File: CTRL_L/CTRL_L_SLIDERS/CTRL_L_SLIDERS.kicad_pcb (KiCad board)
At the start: 2 copper layers, 1 part

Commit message: Finished Volume/Brightness Slider Daugherboard!
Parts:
- removed the REF** at (126.5, 105.5)
- added J1: BM04B-NSHSS-TBT_LF__SN_, BM04B-NSHSS-TBT:BM04BNSHSSTBTLFSN, B.Cu at (190.9, 90.2)
- added REF**: M2.5_2.7mm, MountingHole:MountingHole_2.7mm_M2.5, B.Cu at (154.6, 81.2)
- added REF**: M2.5_2.7mm, MountingHole:MountingHole_2.7mm_M2.5, B.Cu at (154.6, 97.1)
- added VR1: RA2043F-20-10EB1-B10K, RA2043F-20-10EB1-B10K:RA2043F2010EB1B10K, F.Cu at (164.0, 96.2)
- added VR2: RA2043F-20-10EB1-B10K, RA2043F-20-10EB1-B10K:RA2043F2010EB1B10K, F.Cu at (164.0, 84.6)
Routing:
- net GND: track 0.00 -> 70.9 mm, vias 0 -> 1
- net SL_BRI: track 0.00 -> 32.8 mm
- net SL_VOL: track 0.00 -> 29.9 mm
- net +3V3: track 0.00 -> 18.0 mm
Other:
- board outline added: 44.2 x 23.2 mm

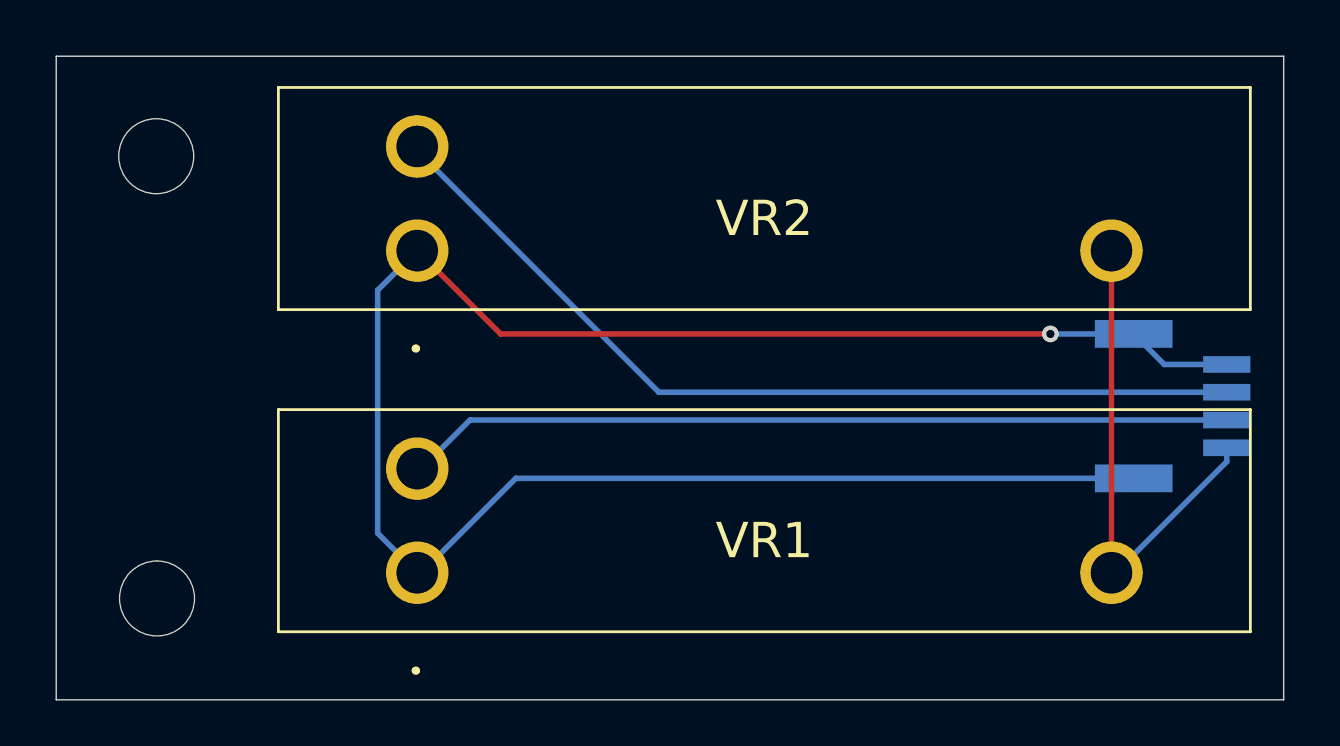
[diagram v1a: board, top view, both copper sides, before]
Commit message: Moved JST Connector and added Test Points
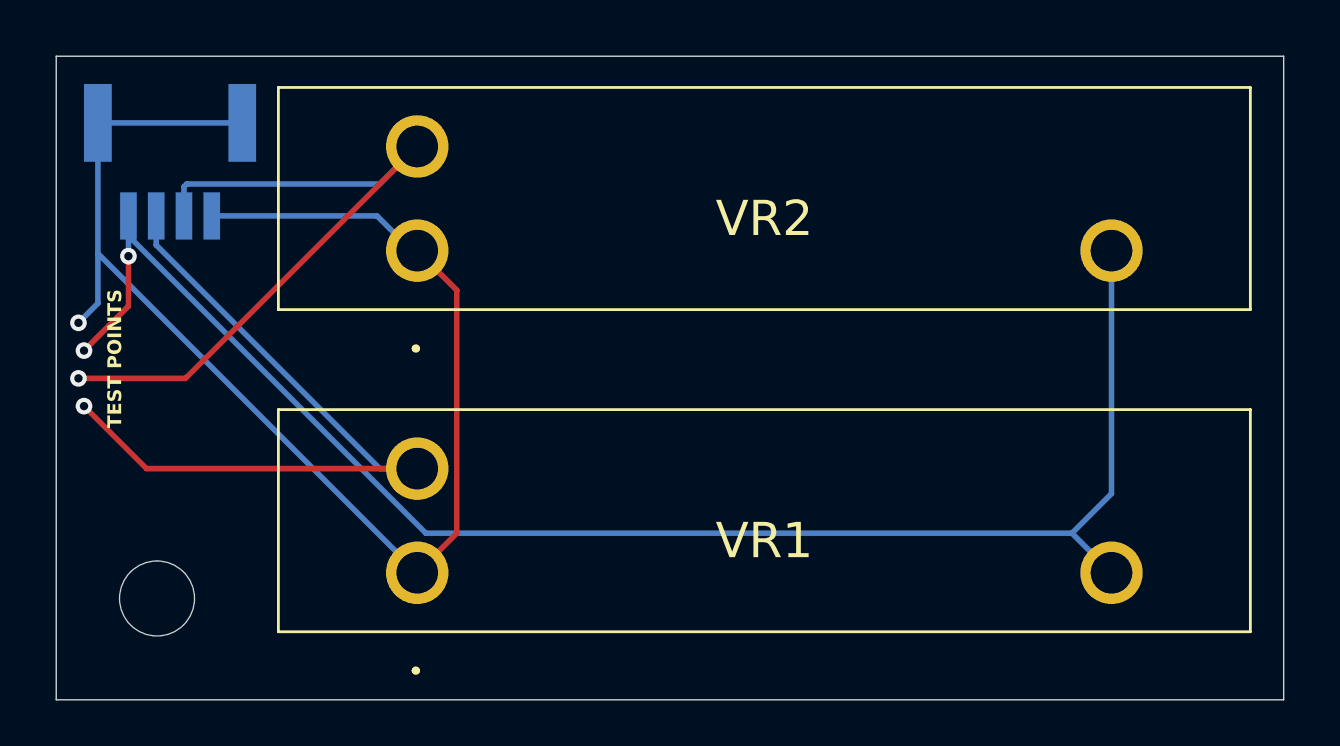
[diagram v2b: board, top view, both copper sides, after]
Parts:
- removed the REF** at (154.6, 81.2)
- moved J1 37.0 mm to (155.1, 81.1), turned to 0 degrees
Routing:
- net +3V3: track 18.0 -> 57.4 mm, vias 0 -> 2
- net GND: track 70.9 -> 49.7 mm
- net SL_BRI: track 32.8 -> 25.7 mm, vias 0 -> 1
- net SL_VOL: track 29.9 -> 26.7 mm, vias 0 -> 1
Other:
- board text added: "TEST POINTS"

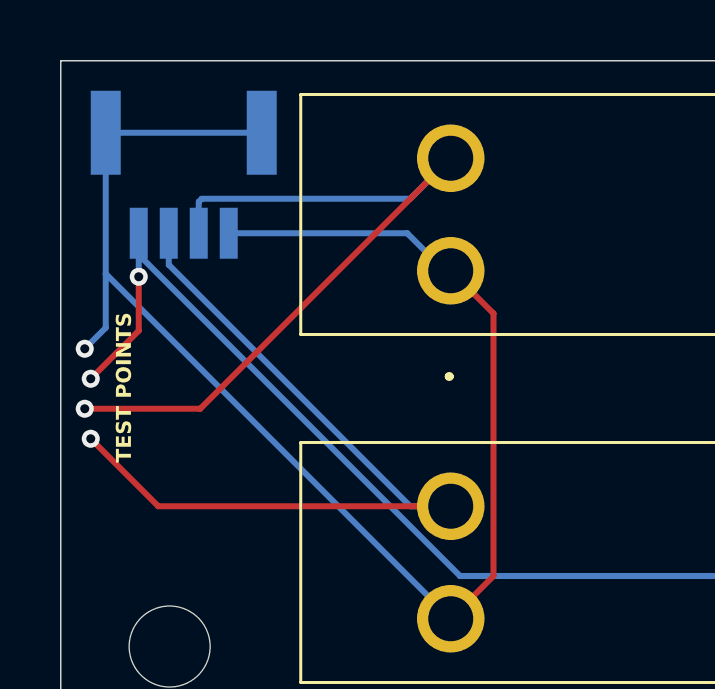
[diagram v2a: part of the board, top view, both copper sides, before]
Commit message: Removed the test points because i dont know what im doing.
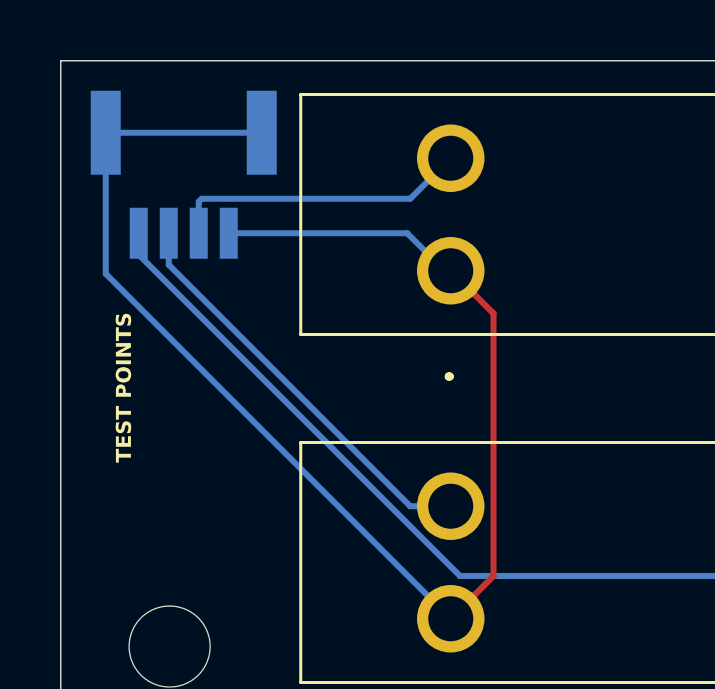
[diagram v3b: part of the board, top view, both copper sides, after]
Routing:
- net SL_BRI: track 25.7 -> 10.1 mm, vias 1 -> 0
- net SL_VOL: track 26.7 -> 13.8 mm, vias 1 -> 0
- net +3V3: track 57.4 -> 51.2 mm, vias 2 -> 0
- net GND: track 49.7 -> 46.7 mm, vias 1 -> 0
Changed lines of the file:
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@@
-		(net "GND")
-	)
-	(via
-		(at 151.8 87.2)
-		(size 0.6)
-		(drill 0.3)
-		(layers "F.Cu" "B.Cu")
-		(net "GND")
-	)
-	(segment
-		(start 164 84.6)
-		(end 163.8 84.6)
-		(width 0.2)
-		(layer "B.Cu")
 		(net "GND")
 	)
@@
 	(segment
 		(start 152.5 84.7)
-		(end 152.5 86.5)
-		(width 0.2)
-		(layer "B.Cu")
-		(net "GND")
-	)
-	(segment
-		(start 152.5 86.5)
-		(end 151.8 87.2)
-		(width 0.2)
-		(layer "B.Cu")
-		(net "GND")
-	)
-	(segment
-		(start 152.5 84.7)
 		(end 164 96.2)
 		(width 0.2)
 		(layer "B.Cu")
 		(net "GND")
-	)
-	(segment
-		(start 155.65 89.2)
-		(end 164 80.85)
-		(width 0.2)
-		(layer "F.Cu")
-		(net "SL_BRI")
-	)
-	(segment
-		(start 151.8 89.2)
-		(end 155.65 89.2)
-		(width 0.2)
-		(layer "F.Cu")
-		(net "SL_BRI")
-	)
-	(via
-		(at 151.8 89.2)
-		(size 0.6)
-		(drill 0.3)
-		(layers "F.Cu" "B.Cu")
-		(net "SL_BRI")
 	)
 	(segment
@@
 	)
 	(segment
-		(start 153.6 86.6)
-		(end 153.6 84.8)
-		(width 0.2)
-		(layer "F.Cu")
-		(net "+3V3")
-	)
-	(segment
-		(start 152 88.2)
-		(end 153.6 86.6)
-		(width 0.2)
-		(layer "F.Cu")
-		(net "+3V3")
-	)
-	(via
-		(at 152 88.2)
-		(size 0.6)
-		(drill 0.3)
-		(layers "F.Cu" "B.Cu")
-		(net "+3V3")
-	)
-	(via
-		(at 153.6 84.8)
-		(size 0.6)
-		(drill 0.3)
-		(layers "F.Cu" "B.Cu")
-		(net "+3V3")
-	)
-	(segment
 		(start 153.6 84.065255)
 		(end 164.309745 94.775)
@@
 	)
 	(segment
-		(start 153.6 83.35)
-		(end 153.6 84.065255)
-		(width 0.2)
-		(layer "B.Cu")
-		(net "+3V3")
-	)
-	(segment
-		(start 153.6 83.35)
-		(end 153.6 84.8)
-		(width 0.2)
-		(layer "B.Cu")
-		(net "+3V3")
-	)
-	(segment
 		(start 164.309745 94.775)
 		(end 187.575 94.775)
@@
 	)
 	(segment
-		(start 164 92.45)
-		(end 154.25 92.45)
-		(width 0.2)
-		(layer "F.Cu")
-		(net "SL_VOL")
-	)
-	(segment
-		(start 154.25 92.45)
-		(end 152 90.2)
-		(width 0.2)
-		(layer "F.Cu")
-		(net "SL_VOL")
-	)
-	(via
-		(at 152 90.2)
-		(size 0.6)
-		(drill 0.3)
-		(layers "F.Cu" "B.Cu")
-		(net "SL_VOL")
-	)
-	(segment

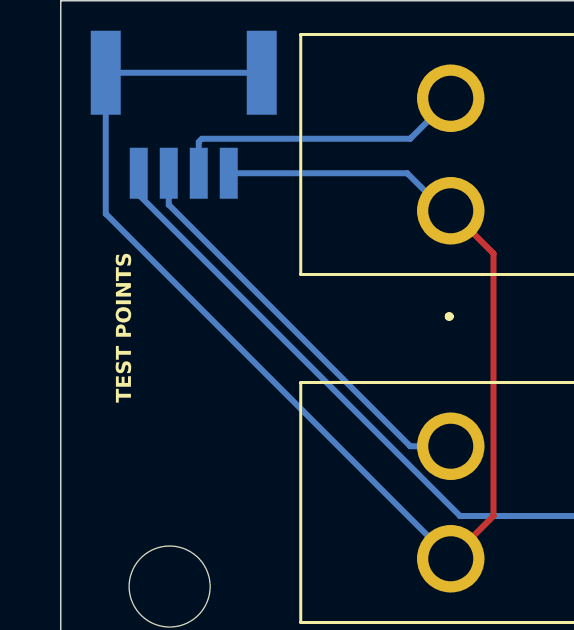
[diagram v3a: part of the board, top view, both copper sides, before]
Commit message: Add LattePandaMu Board files, many fixes to do!
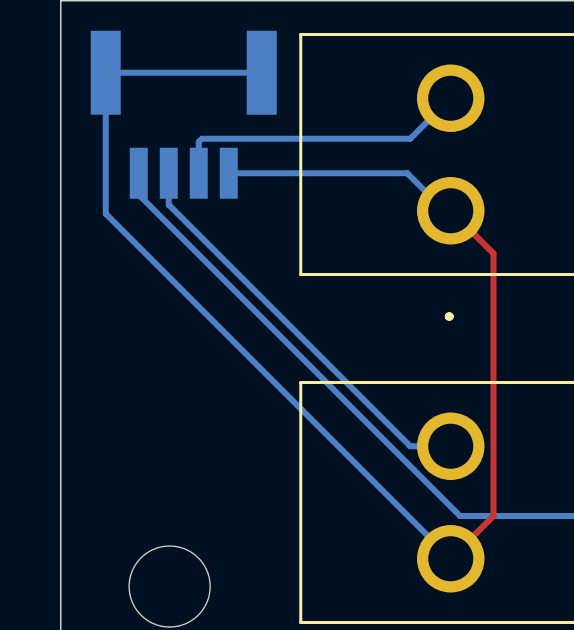
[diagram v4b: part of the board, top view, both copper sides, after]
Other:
- board text removed: "TEST POINTS"
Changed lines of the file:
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@@
 		(layer "Edge.Cuts")
-	)
-	(gr_text "TEST POINTS"
-		(at 153.4 91 90)
-		(layer "F.SilkS")
-		(effects
-			(font
-				(size 0.5 0.5)
-				(thickness 0.125)
-				(bold yes)
-			)
-			(justify left bottom)
-		)
 	)
 	(dimension
